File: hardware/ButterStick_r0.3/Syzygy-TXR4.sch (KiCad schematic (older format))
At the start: 15 parts, among them J8 SYZYGY-TXR-4, Q1 PMBT3904MB, U2 TLV6001DCK

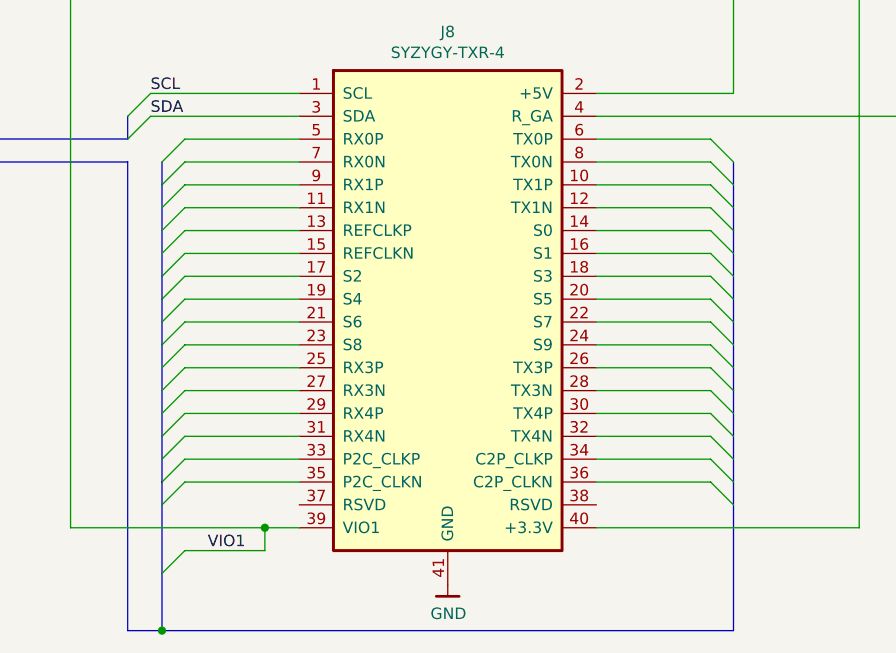
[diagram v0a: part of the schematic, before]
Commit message: hw.r0_3: Update schematics with 85F-5G symbol
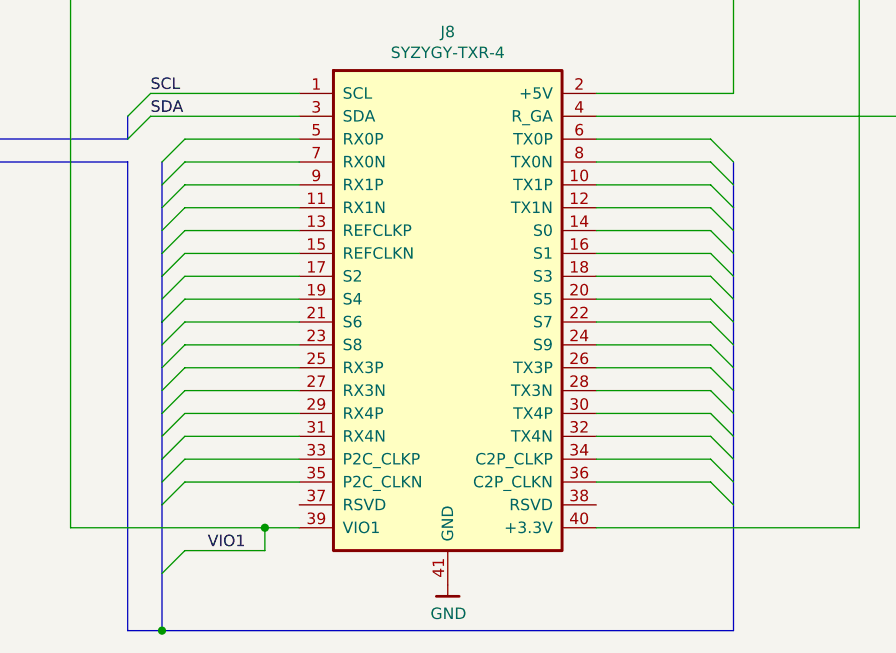
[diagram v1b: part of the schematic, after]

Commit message: hw.r0_3: Start pin assignments for DDR3
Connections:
- net TX1_P: now reaches J8.10 (TX1P)
- net RX1_N: now reaches J8.11 (RX1N)
- net TX1_N: now reaches J8.12 (TX1N)
- net REFCLK_P: now reaches J8.13 (REFCLKP)
- net S0: now reaches J8.14 (S0)
- net REFCLK_N: now reaches J8.15 (REFCLKN)
- net S1: now reaches J8.16 (S1)
- net S2: now reaches J8.17 (S2)
- net S3: now reaches J8.18 (S3)
- net S4: now reaches J8.19 (S4)
- net S5: now reaches J8.20 (S5)
- net S6: now reaches J8.21 (S6)
- net S7: now reaches J8.22 (S7)
- net S8: now reaches J8.23 (S8)
- net S9: now reaches J8.24 (S9)
- net RX3_P: now reaches J8.25 (RX3P)
- net TX3_P: now reaches J8.26 (TX3P)
- net RX3_N: now reaches J8.27 (RX3N)
- net TX3_N: now reaches J8.28 (TX3N)
- net RX4_P: now reaches J8.29 (RX4P)
- net TX4_P: now reaches J8.30 (TX4P)
- net RX4_N: now reaches J8.31 (RX4N)
- net TX4_N: now reaches J8.32 (TX4N)
- net P2C_CLK_P: now reaches J8.33 (P2C_CLKP)
- net C2P_CLK_P: now reaches J8.34 (C2P_CLKP)
- net P2C_CLK_N: now reaches J8.35 (P2C_CLKN)
- net C2P_CLK_N: now reaches J8.36 (C2P_CLKN)
- net RX0_P: now reaches J8.5 (RX0P)
- net TX0_P: now reaches J8.6 (TX0P)
- net RX0_N: now reaches J8.7 (RX0N)
- net TX0_N: now reaches J8.8 (TX0N)
- net RX1_P: now reaches J8.9 (RX1P)
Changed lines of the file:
@@
 $Descr A4 11693 8268
 encoding utf-8
-Sheet 11 18
+Sheet 19 20
 Title "ButterStick"
 Date "2019-06-14"
@@
 	9000 4600 9000 4800
 Wire Bus Line
-	9000 4800 9000 5000
-Wire Bus Line
-	9000 5000 9000 5200
+	9000 4800 9000 4900
+Wire Bus Line
+	9000 4900 9000 5100
+Wire Bus Line
+	9000 5100 9000 5200
 Wire Bus Line
 	9000 5200 9000 5400
@@
 Text Notes 3700 1600 0    50   ~ 0
 Max power dissipation\n400mW
-Text Label 1750 3900 0    50   ~ 0
-{I2C}
-Text Label 1750 4000 0    50   ~ 0
-{SYZYGY_TXR4}
 Text Label 4800 1850 0    50   ~ 0
 VOUT
@@
 Text Label 6450 3800 0    50   ~ 0
 SDA
+Text Label 6600 3900 0    50   ~ 0
+RX0_P
+Text Label 6600 4000 0    50   ~ 0
+RX0_N
+Text Label 6600 4100 0    50   ~ 0
+RX1_P
+Text Label 6600 4200 0    50   ~ 0
+RX1_N
+Text Label 6600 4300 0    50   ~ 0
+REFCLK_P
+Text Label 6600 4400 0    50   ~ 0
+REFCLK_N
+Text Label 6600 4500 0    50   ~ 0
+S2
+Text Label 6600 4600 0    50   ~ 0
+S4
+Text Label 6600 4700 0    50   ~ 0
+S6
+Text Label 6600 4800 0    50   ~ 0
+S8
+Text Label 6600 4900 0    50   ~ 0
+RX3_P
+Text Label 6600 5000 0    50   ~ 0
+RX3_N
+Text Label 6600 5100 0    50   ~ 0
+RX4_P
+Text Label 6600 5200 0    50   ~ 0
+RX4_N
+Text Label 6600 5300 0    50   ~ 0
+P2C_CLK_P
+Text Label 6600 5400 0    50   ~ 0
+P2C_CLK_N
 Text Label 6700 5700 0    50   ~ 0
 VIO1
+Text Label 8900 3900 2    50   ~ 0
+TX0_P
+Text Label 8900 4000 2    50   ~ 0
+TX0_N
+Text Label 8900 4100 2    50   ~ 0
+TX1_P
+Text Label 8900 4200 2    50   ~ 0
+TX1_N
+Text Label 8900 4300 2    50   ~ 0
+S0
+Text Label 8900 4400 2    50   ~ 0
+S1
+Text Label 8900 4500 2    50   ~ 0
+S3
+Text Label 8900 4600 2    50   ~ 0
+S5
+Text Label 8900 4700 2    50   ~ 0
+S7
+Text Label 8900 4800 2    50   ~ 0
+S9
+Text Label 8900 4900 2    50   ~ 0
+TX3_P
+Text Label 8900 5000 2    50   ~ 0
+TX3_N
+Text Label 8900 5100 2    50   ~ 0
+TX4_P
+Text Label 8900 5200 2    50   ~ 0
+TX4_N
+Text Label 8900 5300 2    50   ~ 0
+C2P_CLK_P
+Text Label 8900 5400 2    50   ~ 0
+C2P_CLK_N
 Text HLabel 1400 2150 0    50   Input ~ 0
 VCCIO_PDM
